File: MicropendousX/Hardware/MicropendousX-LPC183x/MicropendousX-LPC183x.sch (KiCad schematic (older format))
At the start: 0 parts

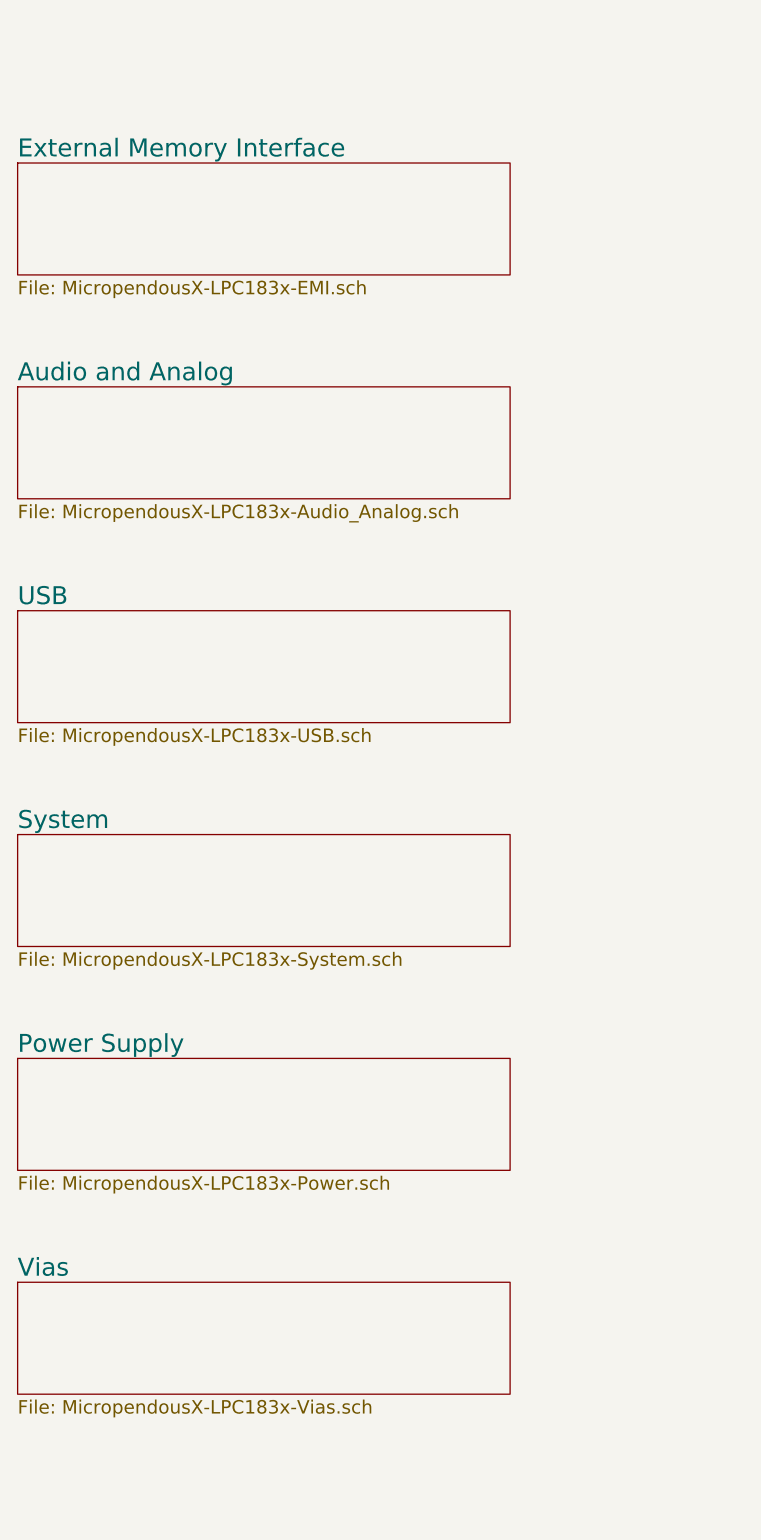
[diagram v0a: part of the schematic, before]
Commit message: Update unfinished LPC183x-based design.
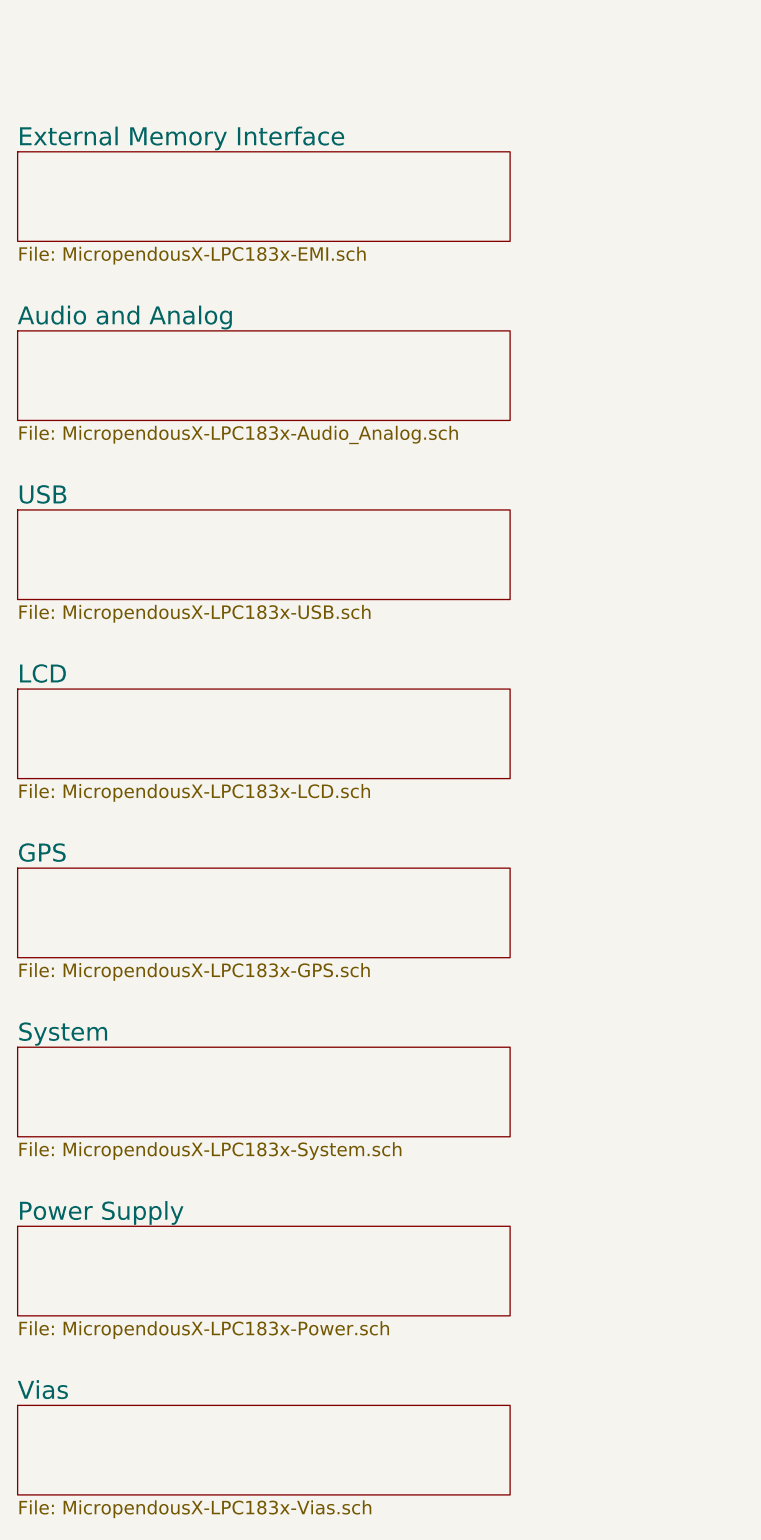
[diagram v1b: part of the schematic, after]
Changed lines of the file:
@@
-EESchema Schematic File Version 2  date 8/15/2011 4:26:38 PM
+EESchema Schematic File Version 2  date 8/20/2011 8:34:09 PM
 LIBS:power
 LIBS:device
@@
 $Descr A4 11700 8267
 encoding utf-8
-Sheet 1 7
+Sheet 1 9
 Title "MicropendousX-LPC183x"
-Date "15 aug 2011"
+Date "21 aug 2011"
 Rev "1.0"
 Comp "Opendous Inc."
@@
 Comment4 "www.MicropendousX.org"
 $EndDescr
+$Sheet
+S 950  3400 2200 400
+U 4E50025A
+F0 "LCD" 80
+F1 "MicropendousX-LPC183x-LCD.sch" 60
+$EndSheet
+$Sheet
+S 950  4200 2200 400
+U 4E4FDEED
+F0 "GPS" 80
+F1 "MicropendousX-LPC183x-GPS.sch" 60
+$EndSheet
 Text Notes 4900 1200 0    70   ~ 0
 Notes:\n- first step in processing interrupts to the Event Router is to\n  disable all interrupts to debounce (Errata 20110701 ER.1)\n- the most useful device in the LPC18xx series is the LPC1830\n  in TQFP100 or TFBGA100.  Pins with a prepended x are pins\n  that exist in the 100-pin packages.  Pins with a prepended y\n  exist on the TFBGA100 package but not the TQFP100
 $Sheet
-S 950  1050 2200 500
+S 950  1000 2200 400
 U 4E1DDD2A
 F0 "External Memory Interface" 80
@@
 $EndSheet
 $Sheet
-S 950  2050 2200 500
+S 950  1800 2200 400
 U 4E1DDD5A
 F0 "Audio and Analog" 80
@@
 $EndSheet
 $Sheet
-S 950  3050 2200 500
+S 950  2600 2200 400
 U 4E1DDD6A
 F0 "USB" 80
@@
 $EndSheet
 $Sheet
-S 950  4050 2200 500
+S 950  5000 2200 400
 U 4E1DDD7A
 F0 "System" 80
@@
 $EndSheet
 $Sheet
-S 950  5050 2200 500
+S 950  5800 2200 400
 U 4E1DDB8A
 F0 "Power Supply" 80
@@
 $EndSheet
 $Sheet
-S 950  6050 2200 500
+S 950  6600 2200 400
 U 4E1DDDAA
 F0 "Vias" 80

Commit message: Updated LPC183x Hardware Design
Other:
- note added: "Notes:\n- The most useful device in the LPC18xx series is the LPC1830\n in TQFP100 or TFBGA100. Pins with a prepended x are pins\n that exist in the 100-pin packages. Pins with a prepended y\n exist on the TFBGA100 package but not the TQFP100\n- Full compatibility with both Opennect-I2S and\n Opennect-SingleEnded-x4 Specifications when\n used with a DC Power Jack. Partial compatibility\n when run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"
- note removed: "Notes:\n- first step in processing interrupts to the Event Router is to\n disable all interrupts to debounce (Errata 20110701 ER.1)\n- the most useful device in the LPC18xx series is the LPC1830\n in TQFP100 or TFBGA100. Pins with a prepended x are pins\n that exist in the 100-pin packages. Pins with a prepended y\n exist on the TFBGA100 package but not the TQFP100"
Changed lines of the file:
@@
-EESchema Schematic File Version 2  date 8/20/2011 8:34:09 PM
+EESchema Schematic File Version 2  date 9/18/2011 3:49:57 PM
 LIBS:power
 LIBS:device
@@
 LIBS:contrib
 LIBS:valves
+LIBS:opendous
+LIBS:Opennect_Schematic_Symbols_Library
 LIBS:MicropendousX-LPC183x-cache
 EELAYER 25  0
@@
 $Descr A4 11700 8267
 encoding utf-8
-Sheet 1 9
+Sheet 1 7
 Title "MicropendousX-LPC183x"
-Date "21 aug 2011"
+Date "18 sep 2011"
 Rev "1.0"
 Comp "Opendous Inc."
@@
 $EndDescr
 $Sheet
-S 950  3400 2200 400
-U 4E50025A
-F0 "LCD" 80
-F1 "MicropendousX-LPC183x-LCD.sch" 60
+S 950  1800 2600 400
+U 4E1DDD5A
+F0 "Opennect_Connector" 80
+F1 "MicropendousX-LPC183x-Opennect_Connector.sch" 60
 $EndSheet
+Text Notes 4900 1200 0    80   ~ 0
+Notes:\n- The most useful device in the LPC18xx series is the LPC1830\n  in TQFP100 or TFBGA100.  Pins with a prepended x are pins\n  that exist in the 100-pin packages.  Pins with a prepended y\n  exist on the TFBGA100 package but not the TQFP100\n- Full compatibility with both Opennect-I2S and\n  Opennect-SingleEnded-x4 Specifications when\n  used with a DC Power Jack.  Partial compatibility\n  when running off USB and/or Li-Ion power supplies.\n- First step in processing interrupts to the Event Router is to\n  disable all interrupts to debounce (Errata 20110701 ER.1)
 $Sheet
-S 950  4200 2200 400
-U 4E4FDEED
-F0 "GPS" 80
-F1 "MicropendousX-LPC183x-GPS.sch" 60
-$EndSheet
-Text Notes 4900 1200 0    70   ~ 0
-Notes:\n- first step in processing interrupts to the Event Router is to\n  disable all interrupts to debounce (Errata 20110701 ER.1)\n- the most useful device in the LPC18xx series is the LPC1830\n  in TQFP100 or TFBGA100.  Pins with a prepended x are pins\n  that exist in the 100-pin packages.  Pins with a prepended y\n  exist on the TFBGA100 package but not the TQFP100
-$Sheet
-S 950  1000 2200 400
+S 950  1000 2600 400
 U 4E1DDD2A
 F0 "External Memory Interface" 80
@@
 $EndSheet
 $Sheet
-S 950  1800 2200 400
-U 4E1DDD5A
-F0 "Audio and Analog" 80
-F1 "MicropendousX-LPC183x-Audio_Analog.sch" 60
-$EndSheet
-$Sheet
-S 950  2600 2200 400
+S 950  2600 2600 400
 U 4E1DDD6A
 F0 "USB" 80
@@
 $EndSheet
 $Sheet
-S 950  5000 2200 400
+S 950  3400 2600 400
 U 4E1DDD7A
 F0 "System" 80
@@
 $EndSheet
 $Sheet
-S 950  5800 2200 400
+S 950  4200 2600 400
 U 4E1DDB8A
 F0 "Power Supply" 80
@@
 $EndSheet
 $Sheet
-S 950  6600 2200 400
+S 950  5000 2600 400
 U 4E1DDDAA
 F0 "Vias" 80

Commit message: Updated LPC183x Hardware Design
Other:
- note added: "<-- Double-click inside a sheet to go to it"
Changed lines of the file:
@@
-EESchema Schematic File Version 2  date 9/18/2011 3:49:57 PM
+EESchema Schematic File Version 2  date 9/18/2011 8:03:49 PM
 LIBS:power
 LIBS:device
@@
 Sheet 1 7
 Title "MicropendousX-LPC183x"
-Date "18 sep 2011"
+Date "19 sep 2011"
 Rev "1.0"
 Comp "Opendous Inc."
@@
 Comment4 "www.MicropendousX.org"
 $EndDescr
+Text Notes 4000 3250 0    200  ~ 0
+<-- Double-click inside a sheet to go to it
 $Sheet
 S 950  1800 2600 400
